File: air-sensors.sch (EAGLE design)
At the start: 13 parts, among them IC1 LM2936Z-3.3, J1 MH-Z19-CO2-NDIR-SENSOR, U1 ESP8266, U2 AM2302

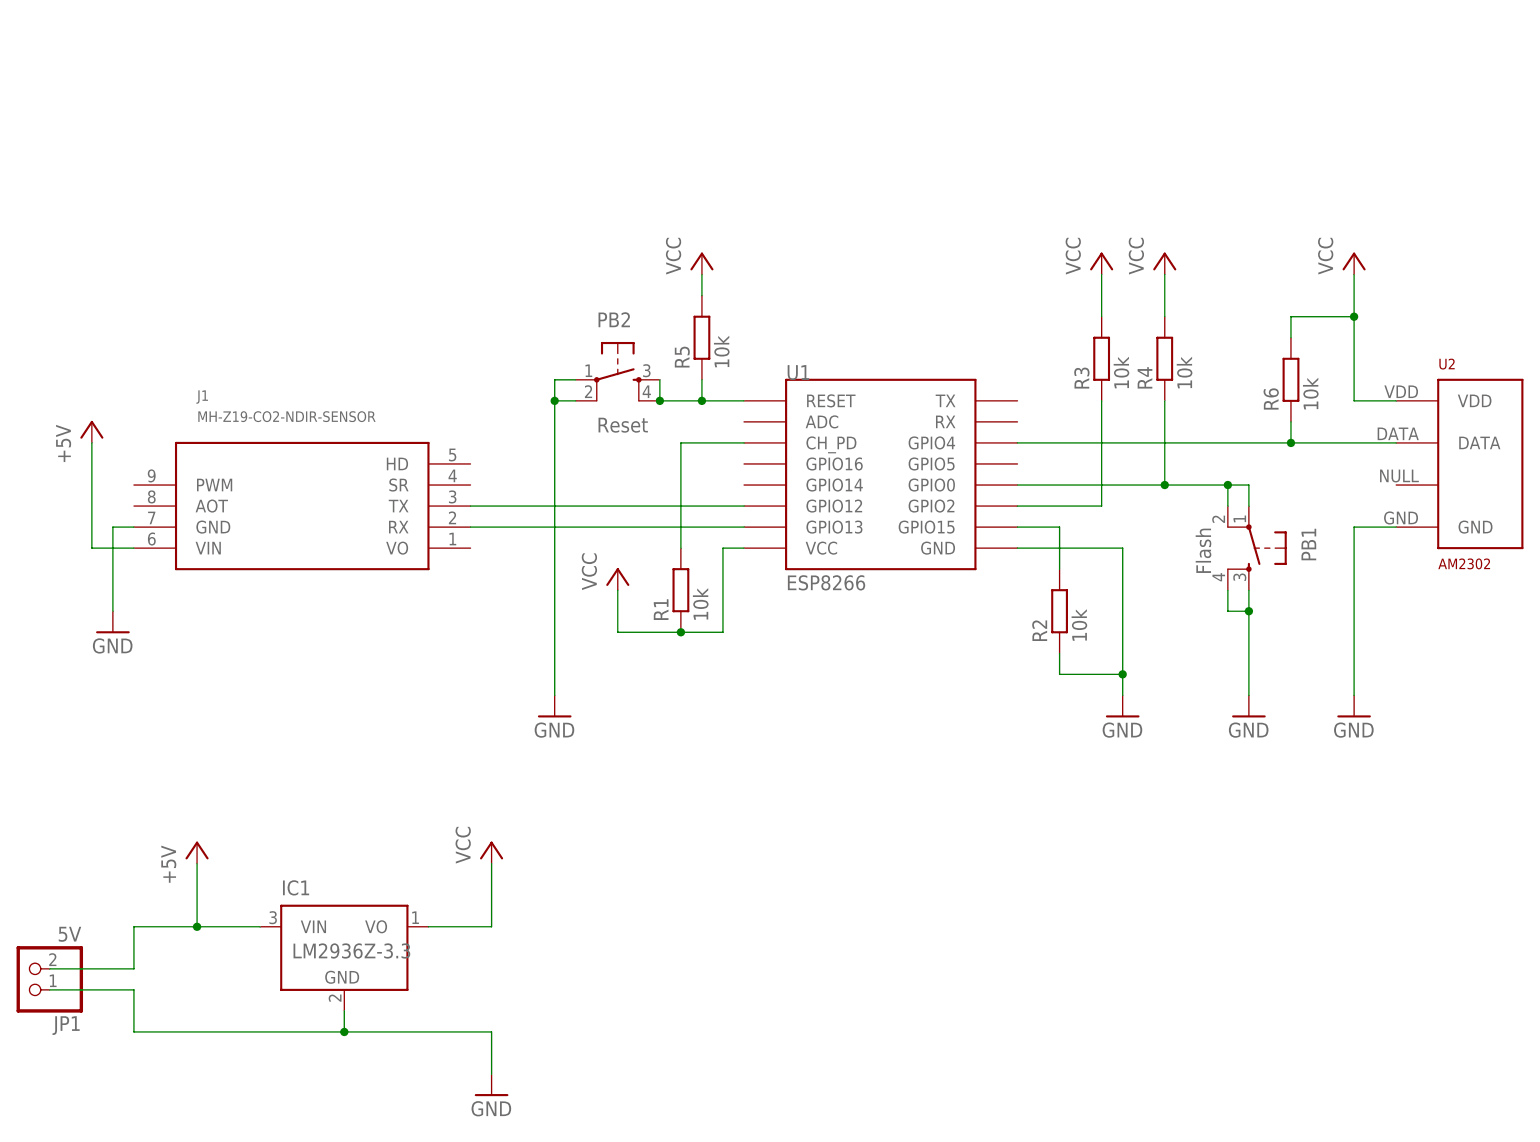
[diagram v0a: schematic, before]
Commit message: Updated schematics: OLED display added.
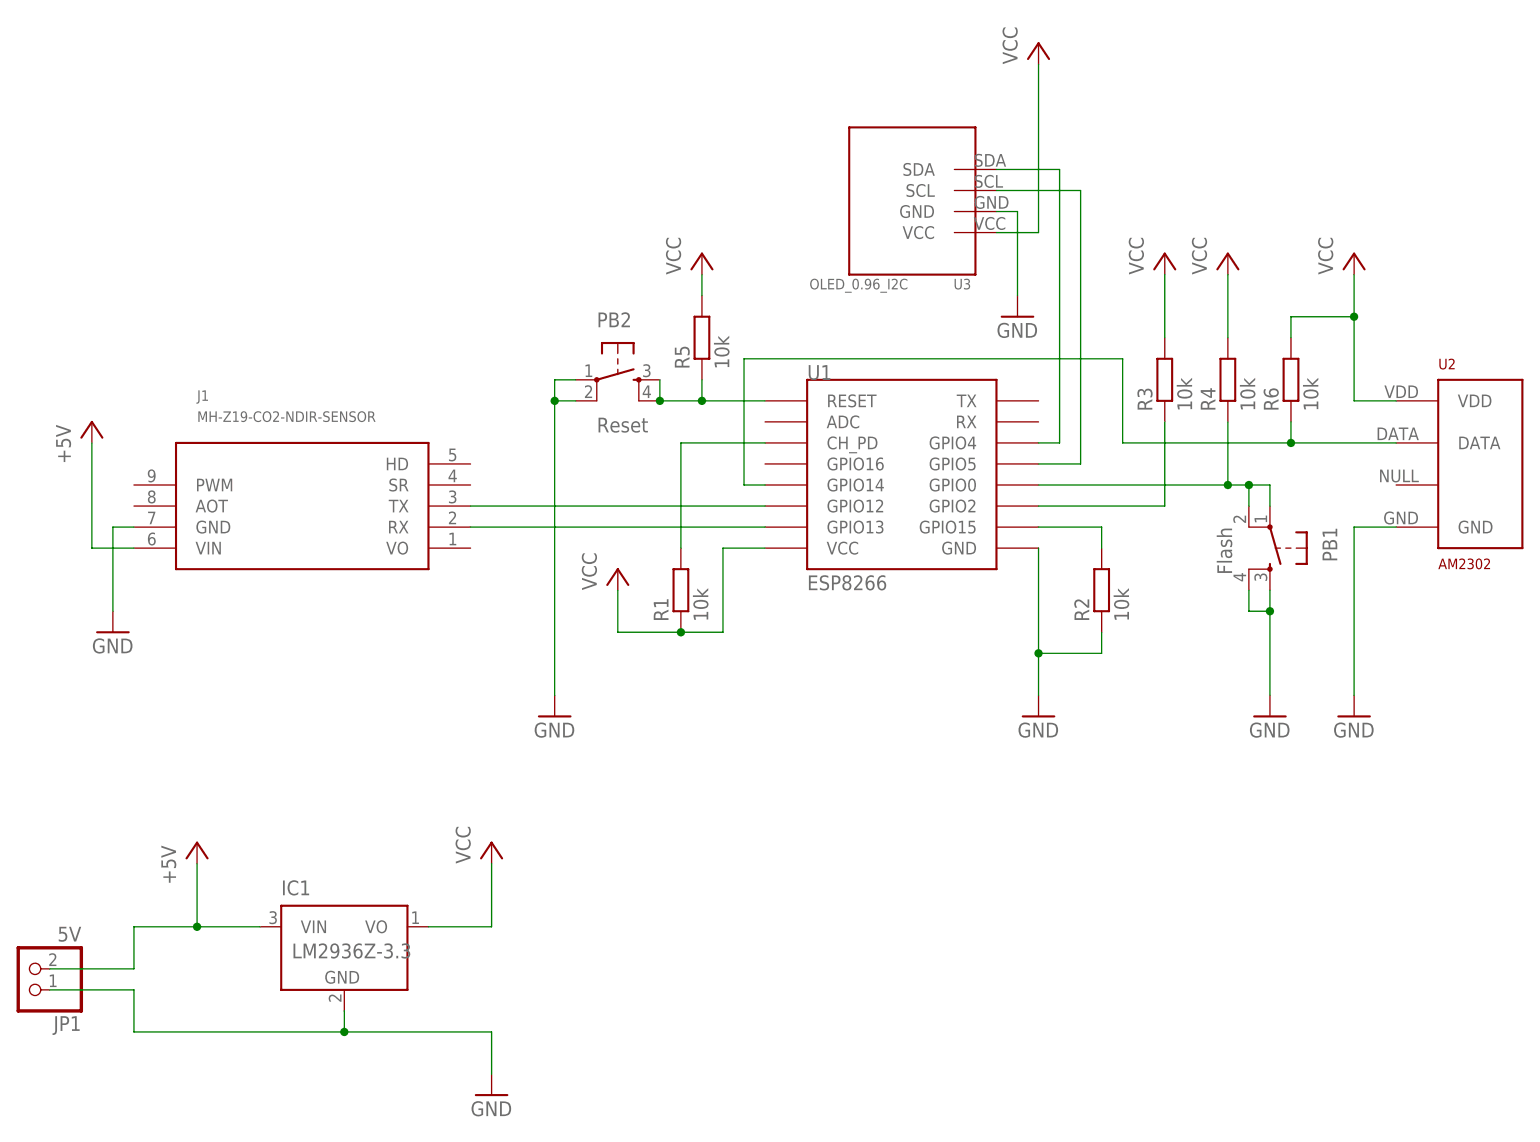
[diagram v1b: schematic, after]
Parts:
- added U3: OLED_0.96_I2C, tft_1.8_1.44_oled_0.96:OLED_0.96_I2C
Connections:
- new net N$11: U1.GPIO5, U3.SCL
- new net N$9: U1.GPIO4, U3.SDA
- net GND: now also U3.GND
- net N$7: now also U1.GPIO14; no longer U1.GPIO4
- net VCC: now also U3.VCC
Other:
- moved on the sheet: PB1, R2, R3, R4, U1
